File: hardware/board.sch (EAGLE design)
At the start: 45 parts, among them IC1 0915BM15A0001, J1 U.FL, U3 BLE113-A, X1 24MHz 8pF 10ppm -20C +70C, X3 MINI-USB-UX60-MB-5ST

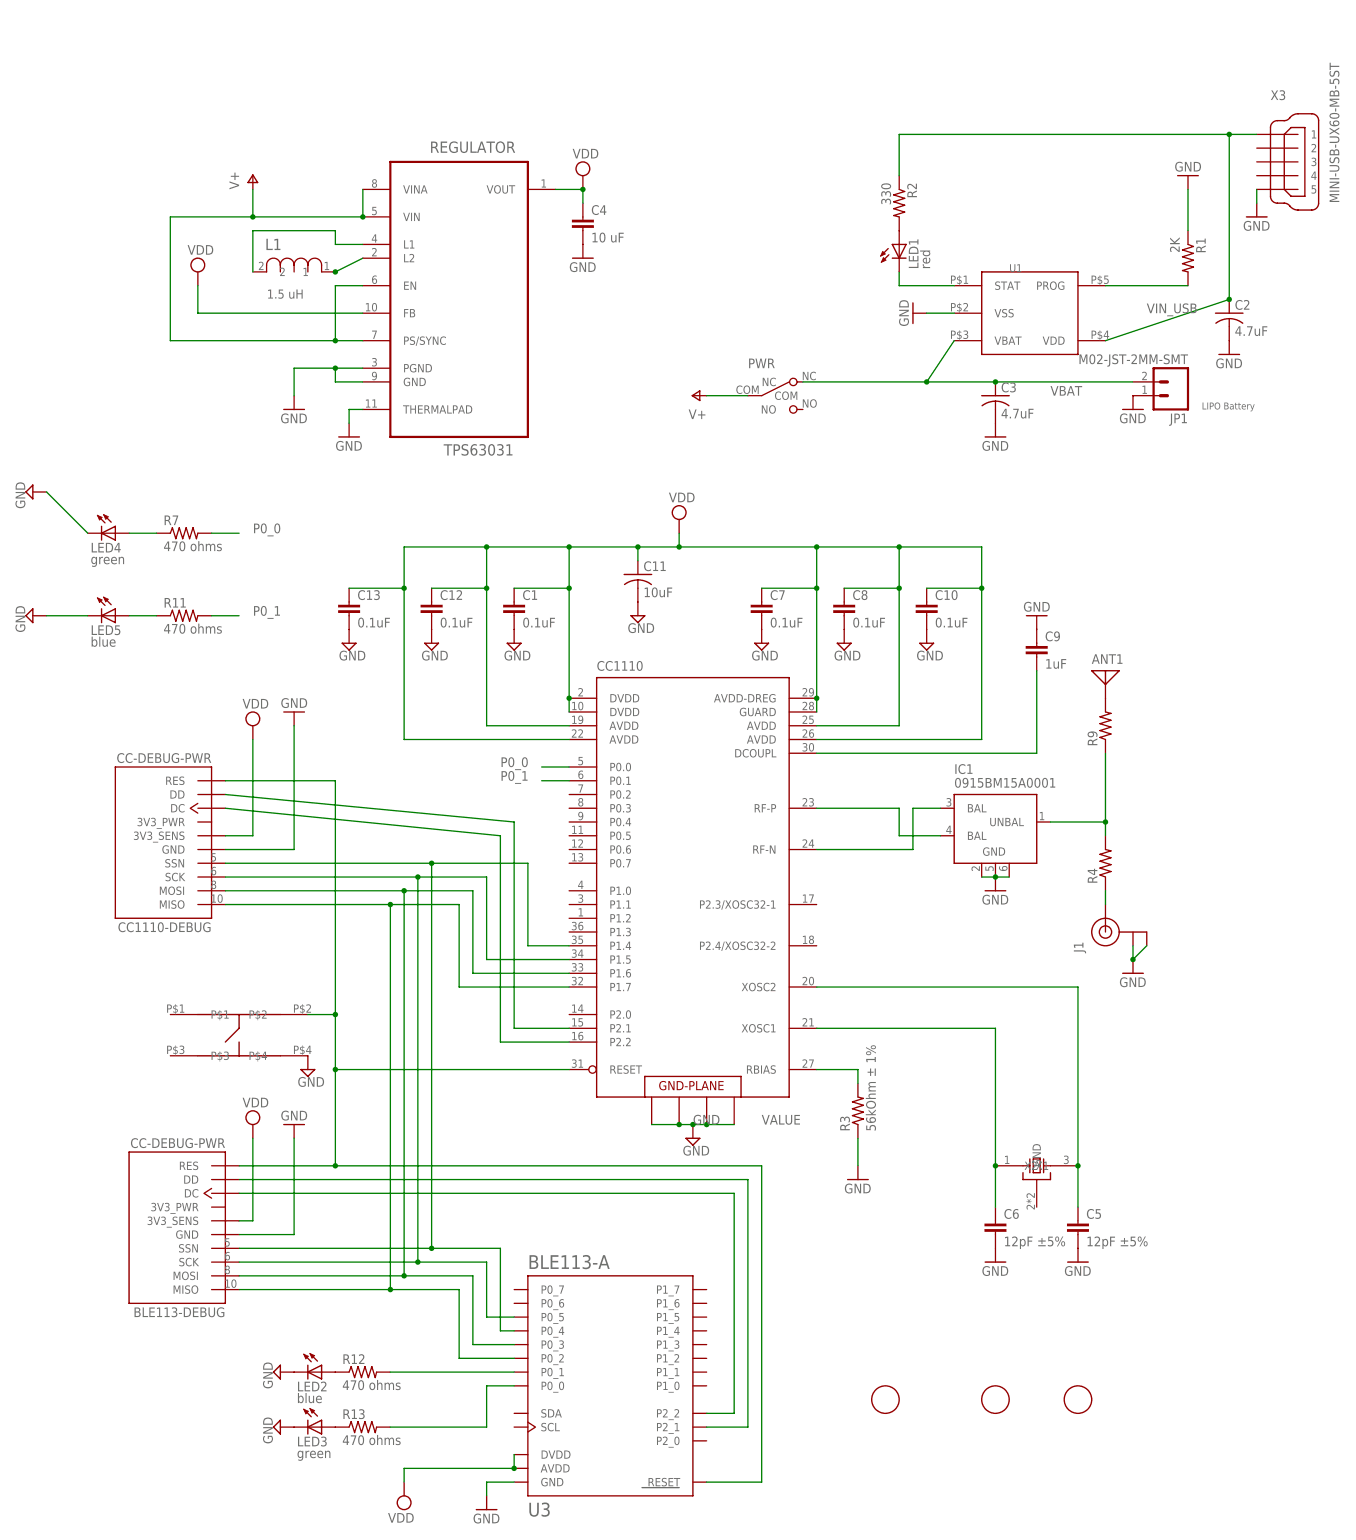
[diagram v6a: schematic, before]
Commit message: New layout for voltage regulator, add 2 pin header for alternate power.
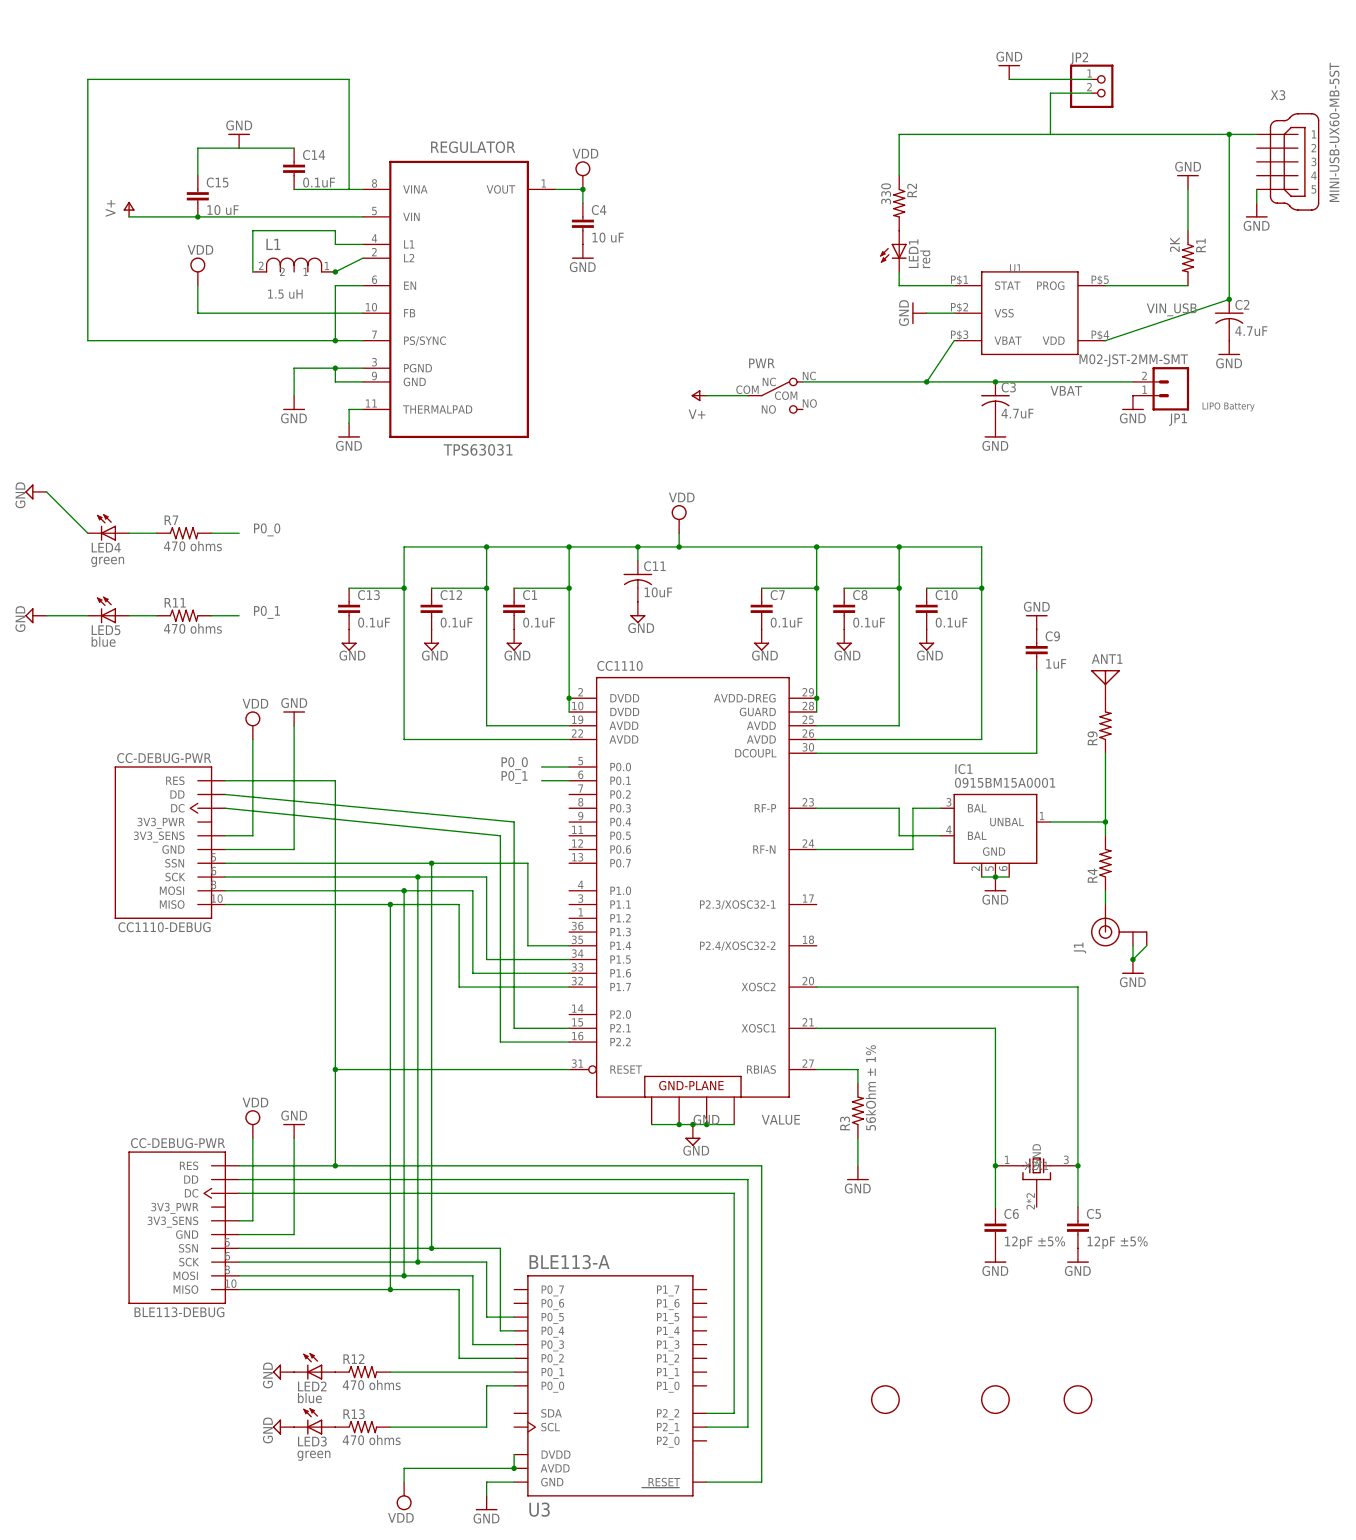
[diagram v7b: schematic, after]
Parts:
- removed U$2: TACTILE_SWITCH, parts:TACTILE_SWITCH
- added C14: 0.1uF, rcl:C-EUC0402
- added C15: 10 uF, rcl:C-EUC0805K
- added JP2: (no value), pinhead:PINHD-1X2
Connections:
- new net N$13: C14.2, REGULATOR.EN, REGULATOR.PS/SYNC, REGULATOR.VINA
- net GND: now also C14.1, C15.1, JP2.1; no longer U$2.P$4
- net RESET: no longer U$2.P$2
- net V+: now also C15.2; no longer REGULATOR.EN, REGULATOR.PS/SYNC, REGULATOR.VINA
- net VIN_USB: now also JP2.2
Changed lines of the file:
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@@
 <?xml version="1.0" encoding="utf-8"?>
 <!DOCTYPE eagle SYSTEM "eagle.dtd">
-<eagle version="7.4.0">
+<eagle version="7.5.0">
 <drawing>
 <settings>
@@
 <part name="PWR" library="parts" deviceset="SW_SLIDE" device=""/>
 <part name="P+1" library="supply1" deviceset="V+" device=""/>
-<part name="U$2" library="parts" deviceset="TACTILE_SWITCH" device=""/>
-<part name="SUPPLY6" library="supply2" deviceset="GND" device=""/>
 <part name="SUPPLY7" library="supply2" deviceset="VDD" device=""/>
 <part name="GND14" library="supply1" deviceset="GND" device=""/>
@@
 <part name="FID2" library="adafruit" deviceset="FIDUCIAL" device=""/>
 <part name="FID3" library="adafruit" deviceset="FIDUCIAL" device=""/>
+<part name="C14" library="rcl" deviceset="C-EU" device="C0402" value="0.1uF"/>
+<part name="GND11" library="supply1" deviceset="GND" device=""/>
+<part name="C15" library="rcl" deviceset="C-EU" device="C0805K" value="10 uF"/>
+<part name="JP2" library="pinhead" deviceset="PINHD-1X2" device=""/>
+<part name="GND12" library="supply1" deviceset="GND" device=""/>
 </parts>
 <sheets>
@@
 <instance part="SUPPLY2" gate="G$1" x="55.88" y="175.26"/>
 <instance part="SUPPLY3" gate="G$1" x="-15.24" y="157.48"/>
-<instance part="P+2" gate="1" x="-5.08" y="175.26"/>
+<instance part="P+2" gate="1" x="-27.94" y="170.18"/>
 <instance part="SUPPLY5" gate="GND" x="76.2" y="-2.54"/>
 <instance part="J1" gate="G$1" x="152.4" y="35.56" rot="R90"/>
@@
 <instance part="PWR" gate="G$1" x="93.98" y="134.62"/>
 <instance part="P+1" gate="1" x="76.2" y="134.62" rot="R90"/>
-<instance part="U$2" gate="G$1" x="-5.08" y="17.78"/>
-<instance part="SUPPLY6" gate="GND" x="5.08" y="10.16"/>
 <instance part="SUPPLY7" gate="G$1" x="-5.08" y="0"/>
 <instance part="GND14" gate="1" x="2.54" y="0" rot="R180"/>
@@
 <instance part="FID2" gate="G$1" x="132.08" y="-50.8"/>
 <instance part="FID3" gate="G$1" x="147.32" y="-50.8"/>
+<instance part="C14" gate="G$1" x="2.54" y="177.8"/>
+<instance part="GND11" gate="1" x="-7.62" y="182.88" rot="R180"/>
+<instance part="C15" gate="G$1" x="-15.24" y="172.72"/>
+<instance part="JP2" gate="G$1" x="152.4" y="190.5"/>
+<instance part="GND12" gate="1" x="134.62" y="195.58" rot="R180"/>
 </instances>
 <busses>
@@
 </segment>
 <segment>
-<pinref part="U$2" gate="G$1" pin="P$4"/>
-<pinref part="SUPPLY6" gate="GND" pin="GND"/>
-</segment>
-<segment>
 <pinref part="BLE113-DEBUG" gate="G$1" pin="GND"/>
 <pinref part="GND14" gate="1" pin="GND"/>
@@
 <junction x="157.48" y="30.48"/>
 <wire x1="157.48" y1="30.48" x2="157.48" y2="33.02" width="0.1524" layer="91"/>
+</segment>
+<segment>
+<pinref part="C14" gate="G$1" pin="1"/>
+<pinref part="GND11" gate="1" pin="GND"/>
+<wire x1="2.54" y1="180.34" x2="-7.62" y2="180.34" width="0.1524" layer="91"/>
+<pinref part="C15" gate="G$1" pin="1"/>
+<wire x1="-15.24" y1="175.26" x2="-15.24" y2="180.34" width="0.1524" layer="91"/>
+<wire x1="-15.24" y1="180.34" x2="-7.62" y2="180.34" width="0.1524" layer="91"/>
+</segment>
+<segment>
+<pinref part="JP2" gate="G$1" pin="1"/>
+<pinref part="GND12" gate="1" pin="GND"/>
+<wire x1="149.86" y1="193.04" x2="134.62" y2="193.04" width="0.1524" layer="91"/>
 </segment>
 </net>
@@
 <pinref part="R2" gate="G$1" pin="1"/>
 <wire x1="114.3" y1="175.26" x2="114.3" y2="182.88" width="0.1524" layer="91"/>
-<wire x1="114.3" y1="182.88" x2="175.26" y2="182.88" width="0.1524" layer="91"/>
+<wire x1="114.3" y1="182.88" x2="142.24" y2="182.88" width="0.1524" layer="91"/>
 <junction x="175.26" y="182.88"/>
+<wire x1="142.24" y1="182.88" x2="175.26" y2="182.88" width="0.1524" layer="91"/>
+<wire x1="142.24" y1="182.88" x2="142.24" y2="190.5" width="0.1524" layer="91"/>
+<pinref part="JP2" gate="G$1" pin="2"/>
+<wire x1="142.24" y1="190.5" x2="149.86" y2="190.5" width="0.1524" layer="91"/>
 </segment>
 </net>
@@
 <net name="V+" class="0">
 <segment>
+<pinref part="P+2" gate="1" pin="V+"/>
 <pinref part="REGULATOR" gate="A" pin="VIN"/>
-<pinref part="REGULATOR" gate="A" pin="VINA"/>
-<wire x1="15.24" y1="167.64" x2="15.24" y2="172.72" width="0.1524" layer="91"/>
-<wire x1="15.24" y1="167.64" x2="-5.08" y2="167.64" width="0.1524" layer="91"/>
-<wire x1="-5.08" y1="167.64" x2="-20.32" y2="167.64" width="0.1524" layer="91"/>
-<wire x1="-20.32" y1="167.64" x2="-20.32" y2="144.78" width="0.1524" layer="91"/>
-<junction x="15.24" y="167.64"/>
-<pinref part="REGULATOR" gate="A" pin="PS/SYNC"/>
-<wire x1="-20.32" y1="144.78" x2="10.16" y2="144.78" width="0.1524" layer="91"/>
-<pinref part="REGULATOR" gate="A" pin="EN"/>
-<wire x1="10.16" y1="144.78" x2="15.24" y2="144.78" width="0.1524" layer="91"/>
-<wire x1="15.24" y1="154.94" x2="10.16" y2="154.94" width="0.1524" layer="91"/>
-<wire x1="10.16" y1="154.94" x2="10.16" y2="144.78" width="0.1524" layer="91"/>
-<junction x="10.16" y="144.78"/>
-<pinref part="P+2" gate="1" pin="V+"/>
-<wire x1="-5.08" y1="167.64" x2="-5.08" y2="172.72" width="0.1524" layer="91"/>
-<junction x="-5.08" y="167.64"/>
+<wire x1="15.24" y1="167.64" x2="-15.24" y2="167.64" width="0.1524" layer="91"/>
+<pinref part="C15" gate="G$1" pin="2"/>
+<junction x="-15.24" y="167.64"/>
+<wire x1="-15.24" y1="167.64" x2="-27.94" y2="167.64" width="0.1524" layer="91"/>
 </segment>
 <segment>
@@
 <wire x1="-7.62" y1="-7.62" x2="10.16" y2="-7.62" width="0.1524" layer="91"/>
 <wire x1="10.16" y1="-7.62" x2="10.16" y2="10.16" width="0.1524" layer="91"/>
-<pinref part="U$2" gate="G$1" pin="P$2"/>
-<wire x1="10.16" y1="10.16" x2="10.16" y2="20.32" width="0.1524" layer="91"/>
-<wire x1="10.16" y1="20.32" x2="5.08" y2="20.32" width="0.1524" layer="91"/>
 <pinref part="CC1110-DEBUG" gate="G$1" pin="RES"/>
 <wire x1="-10.16" y1="63.5" x2="10.16" y2="63.5" width="0.1524" layer="91"/>
-<wire x1="10.16" y1="20.32" x2="10.16" y2="63.5" width="0.1524" layer="91"/>
-<junction x="10.16" y="20.32"/>
+<wire x1="10.16" y1="10.16" x2="10.16" y2="63.5" width="0.1524" layer="91"/>
 <pinref part="CC1110" gate="G$1" pin="RESET"/>
 <wire x1="53.34" y1="10.16" x2="10.16" y2="10.16" width="0.1524" layer="91"/>
@@
 </segment>
 </net>
+<net name="N$13" class="0">
+<segment>
+<pinref part="REGULATOR" gate="A" pin="PS/SYNC"/>
+<wire x1="-35.56" y1="144.78" x2="10.16" y2="144.78" width="0.1524" layer="91"/>
+<pinref part="REGULATOR" gate="A" pin="EN"/>
+<wire x1="10.16" y1="144.78" x2="15.24" y2="144.78" width="0.1524" layer="91"/>
+<wire x1="15.24" y1="154.94" x2="10.16" y2="154.94" width="0.1524" layer="91"/>
+<wire x1="10.16" y1="154.94" x2="10.16" y2="144.78" width="0.1524" layer="91"/>
+<junction x="10.16" y="144.78"/>
+<wire x1="-35.56" y1="144.78" x2="-35.56" y2="193.04" width="0.1524" layer="91"/>
+<pinref part="REGULATOR" gate="A" pin="VINA"/>
+<pinref part="C14" gate="G$1" pin="2"/>
+<wire x1="15.24" y1="172.72" x2="12.7" y2="172.72" width="0.1524" layer="91"/>
+<wire x1="12.7" y1="172.72" x2="2.54" y2="172.72" width="0.1524" layer="91"/>
+<wire x1="-35.56" y1="193.04" x2="12.7" y2="193.04" width="0.1524" layer="91"/>
+<wire x1="12.7" y1="193.04" x2="12.7" y2="172.72" width="0.1524" layer="91"/>
+</segment>
+</net>

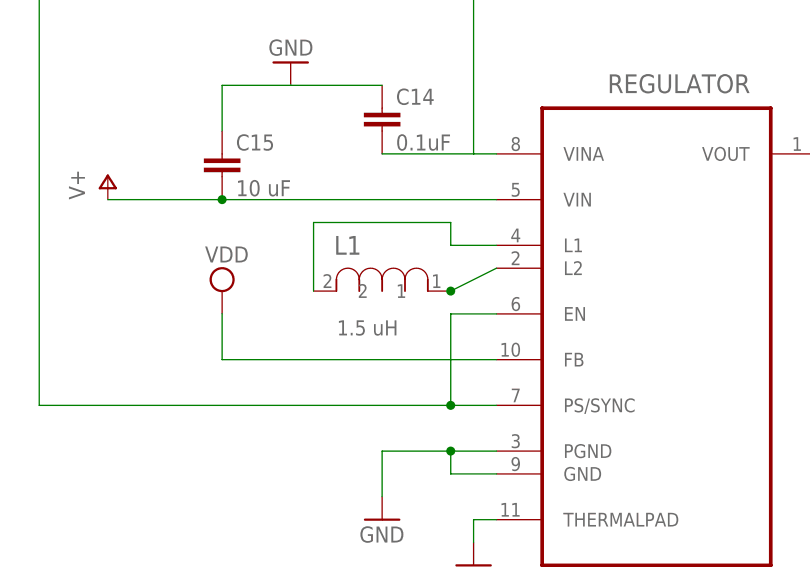
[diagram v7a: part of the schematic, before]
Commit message: Adding higher rated inductor
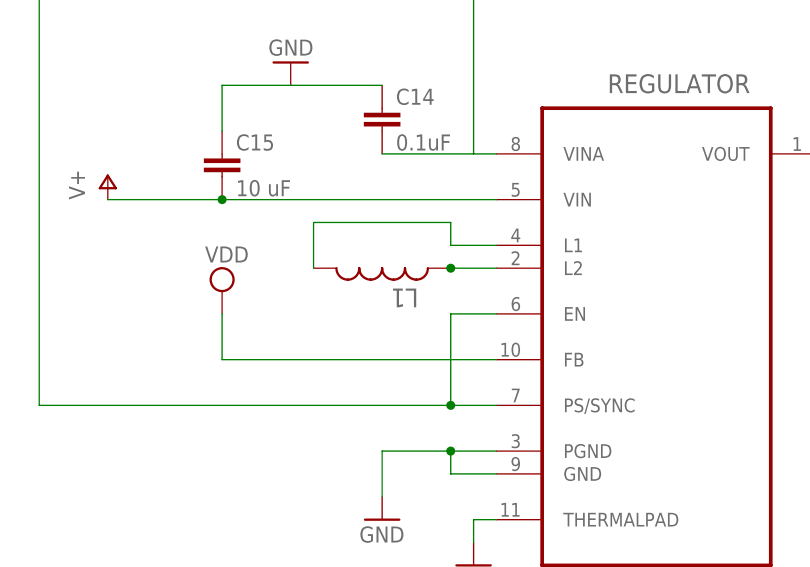
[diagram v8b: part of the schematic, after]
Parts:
- L1: device Bourns_By_element14_Batch_1:PM0603-R12J-RC -> rcl:L-USL2825P; MPN MLF1608A1R5KTD25 -> (none); SUPPLIER Mouser -> (none)
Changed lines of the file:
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@@
 <part name="GND7" library="supply1" deviceset="GND" device=""/>
 <part name="GND8" library="supply1" deviceset="GND" device=""/>
-<part name="L1" library="Bourns_By_element14_Batch_1" deviceset="PM0603-R12J-RC" device="" value="1.5 uH">
-<attribute name="MPN" value="MLF1608A1R5KTD25"/>
-<attribute name="OC_FARNELL" value=""/>
-<attribute name="OC_NEWARK" value=""/>
-<attribute name="SUPPLIER" value="Mouser"/>
-</part>
+<part name="L1" library="rcl" deviceset="L-US" device="L2825P" value="1.5 uH"/>
 <part name="C4" library="rcl" deviceset="C-EU" device="C0805K" value="10 uF"/>
 <part name="GND9" library="supply1" deviceset="GND" device=""/>
@@
 <instance part="GND7" gate="1" x="2.54" y="132.08"/>
 <instance part="GND8" gate="1" x="12.7" y="127"/>
-<instance part="L1" gate="A" x="-5.08" y="157.48" smashed="yes">
-<attribute name="NAME" x="-2.8194" y="161.5186" size="2.0828" layer="95" ratio="10" rot="SR0"/>
-<attribute name="VALUE" x="-2.4892" y="152.5524" size="1.6764" layer="96" ratio="10" rot="SR0"/>
+<instance part="L1" gate="G$1" x="2.54" y="160.02" smashed="yes" rot="R270">
+<attribute name="NAME" x="6.5786" y="157.7594" size="2.0828" layer="95" ratio="10" rot="SR180"/>
 </instance>
 <instance part="C4" gate="G$1" x="55.88" y="167.64"/>
@@
 <segment>
 <pinref part="REGULATOR" gate="A" pin="L2"/>
-<pinref part="L1" gate="A" pin="1"/>
-<wire x1="10.16" y1="157.48" x2="15.24" y2="160.02" width="0.1524" layer="91"/>
-<junction x="10.16" y="157.48"/>
+<pinref part="L1" gate="G$1" pin="1"/>
+<wire x1="10.16" y1="160.02" x2="15.24" y2="160.02" width="0.1524" layer="91"/>
+<junction x="10.16" y="160.02"/>
 </segment>
 </net>
@@
 <wire x1="15.24" y1="162.56" x2="10.16" y2="162.56" width="0.1524" layer="91"/>
 <wire x1="10.16" y1="162.56" x2="10.16" y2="165.1" width="0.1524" layer="91"/>
-<pinref part="L1" gate="A" pin="2"/>
+<pinref part="L1" gate="G$1" pin="2"/>
 <wire x1="10.16" y1="165.1" x2="-5.08" y2="165.1" width="0.1524" layer="91"/>
-<wire x1="-5.08" y1="165.1" x2="-5.08" y2="157.48" width="0.1524" layer="91"/>
-</segment>
-</net>
+<wire x1="-5.08" y1="165.1" x2="-5.08" y2="160.02" width="0.1524" layer="91"/>
+</segment>
+</net>
